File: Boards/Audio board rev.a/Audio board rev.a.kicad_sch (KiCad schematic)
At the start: 65 parts

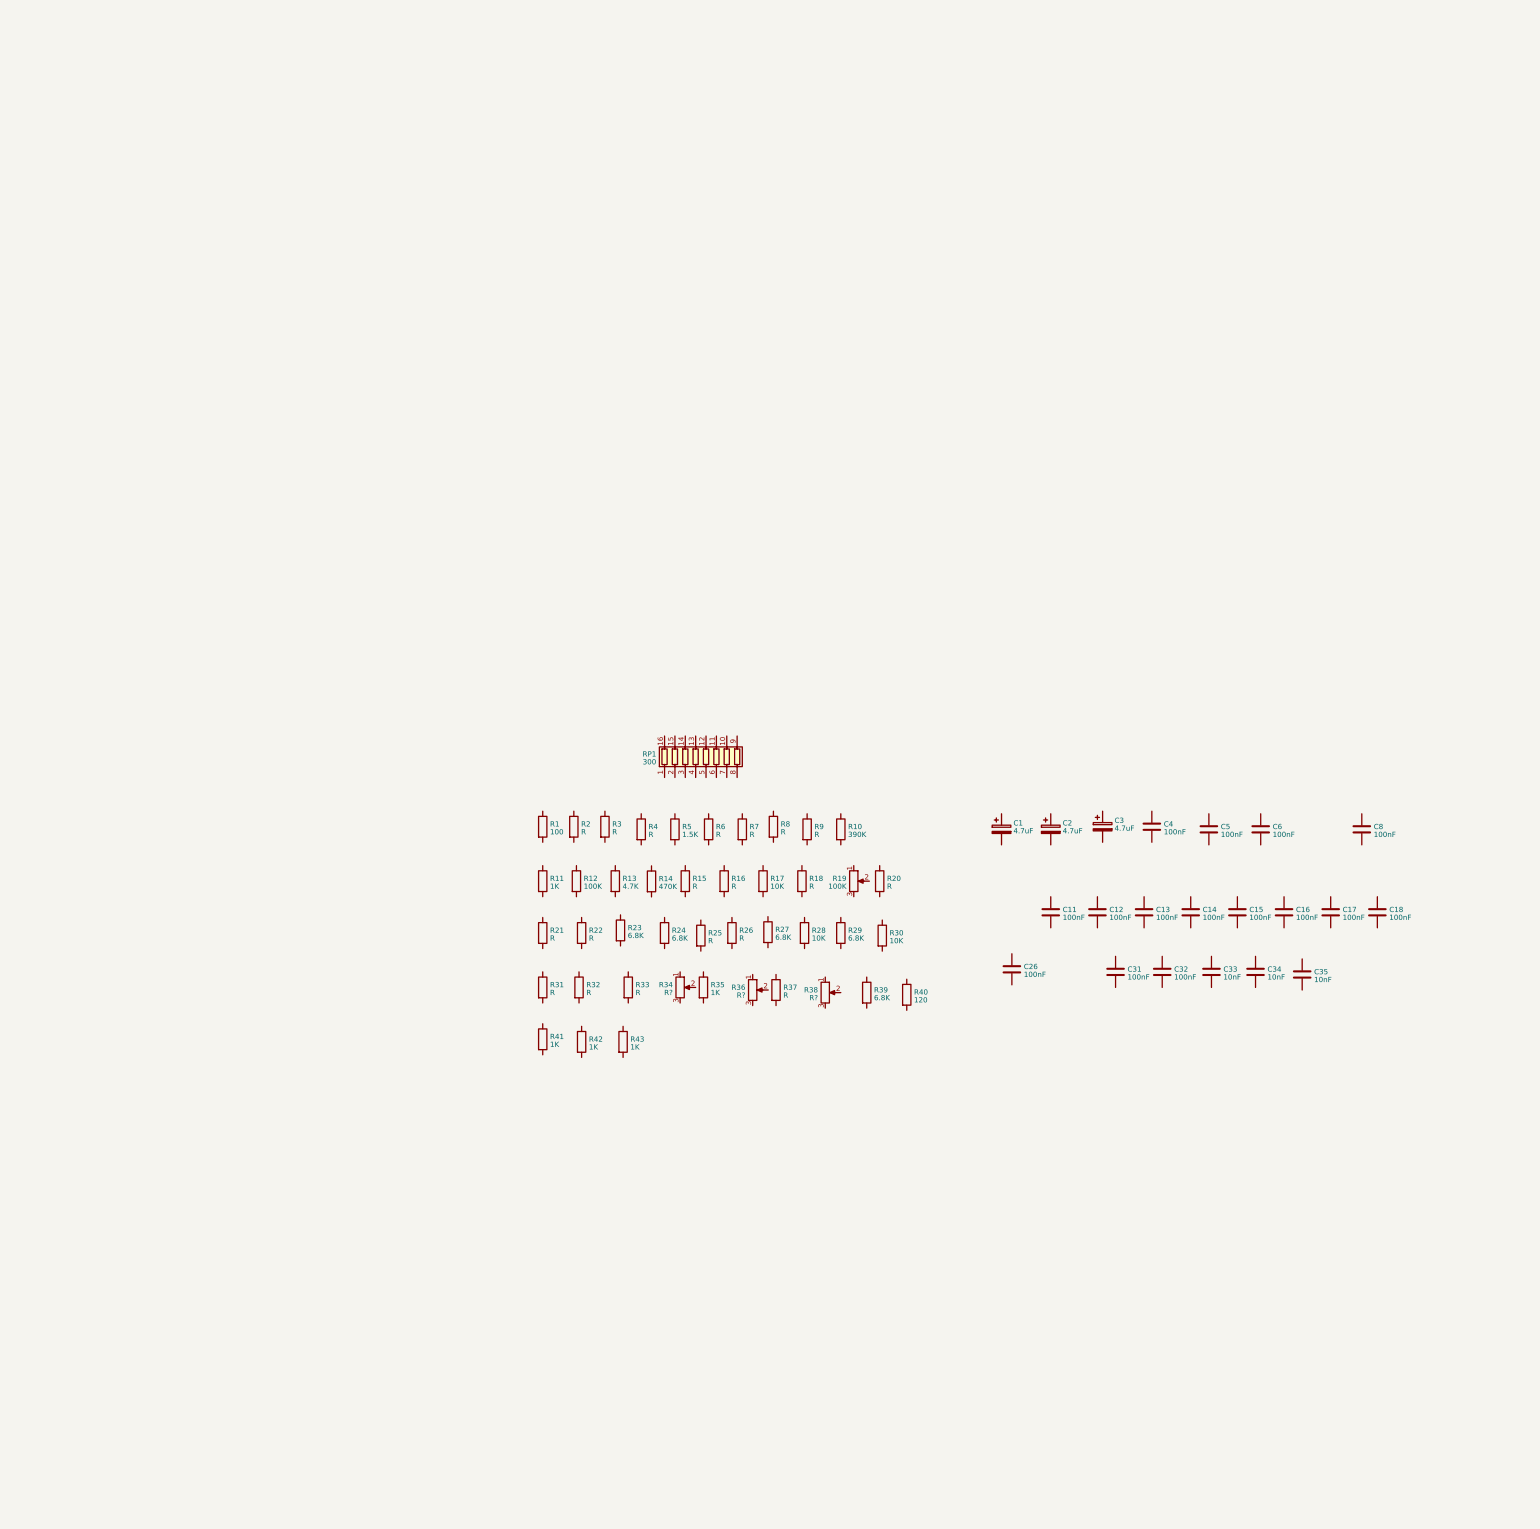
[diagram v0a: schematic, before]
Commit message: audio board rev a agc circuit probably complete
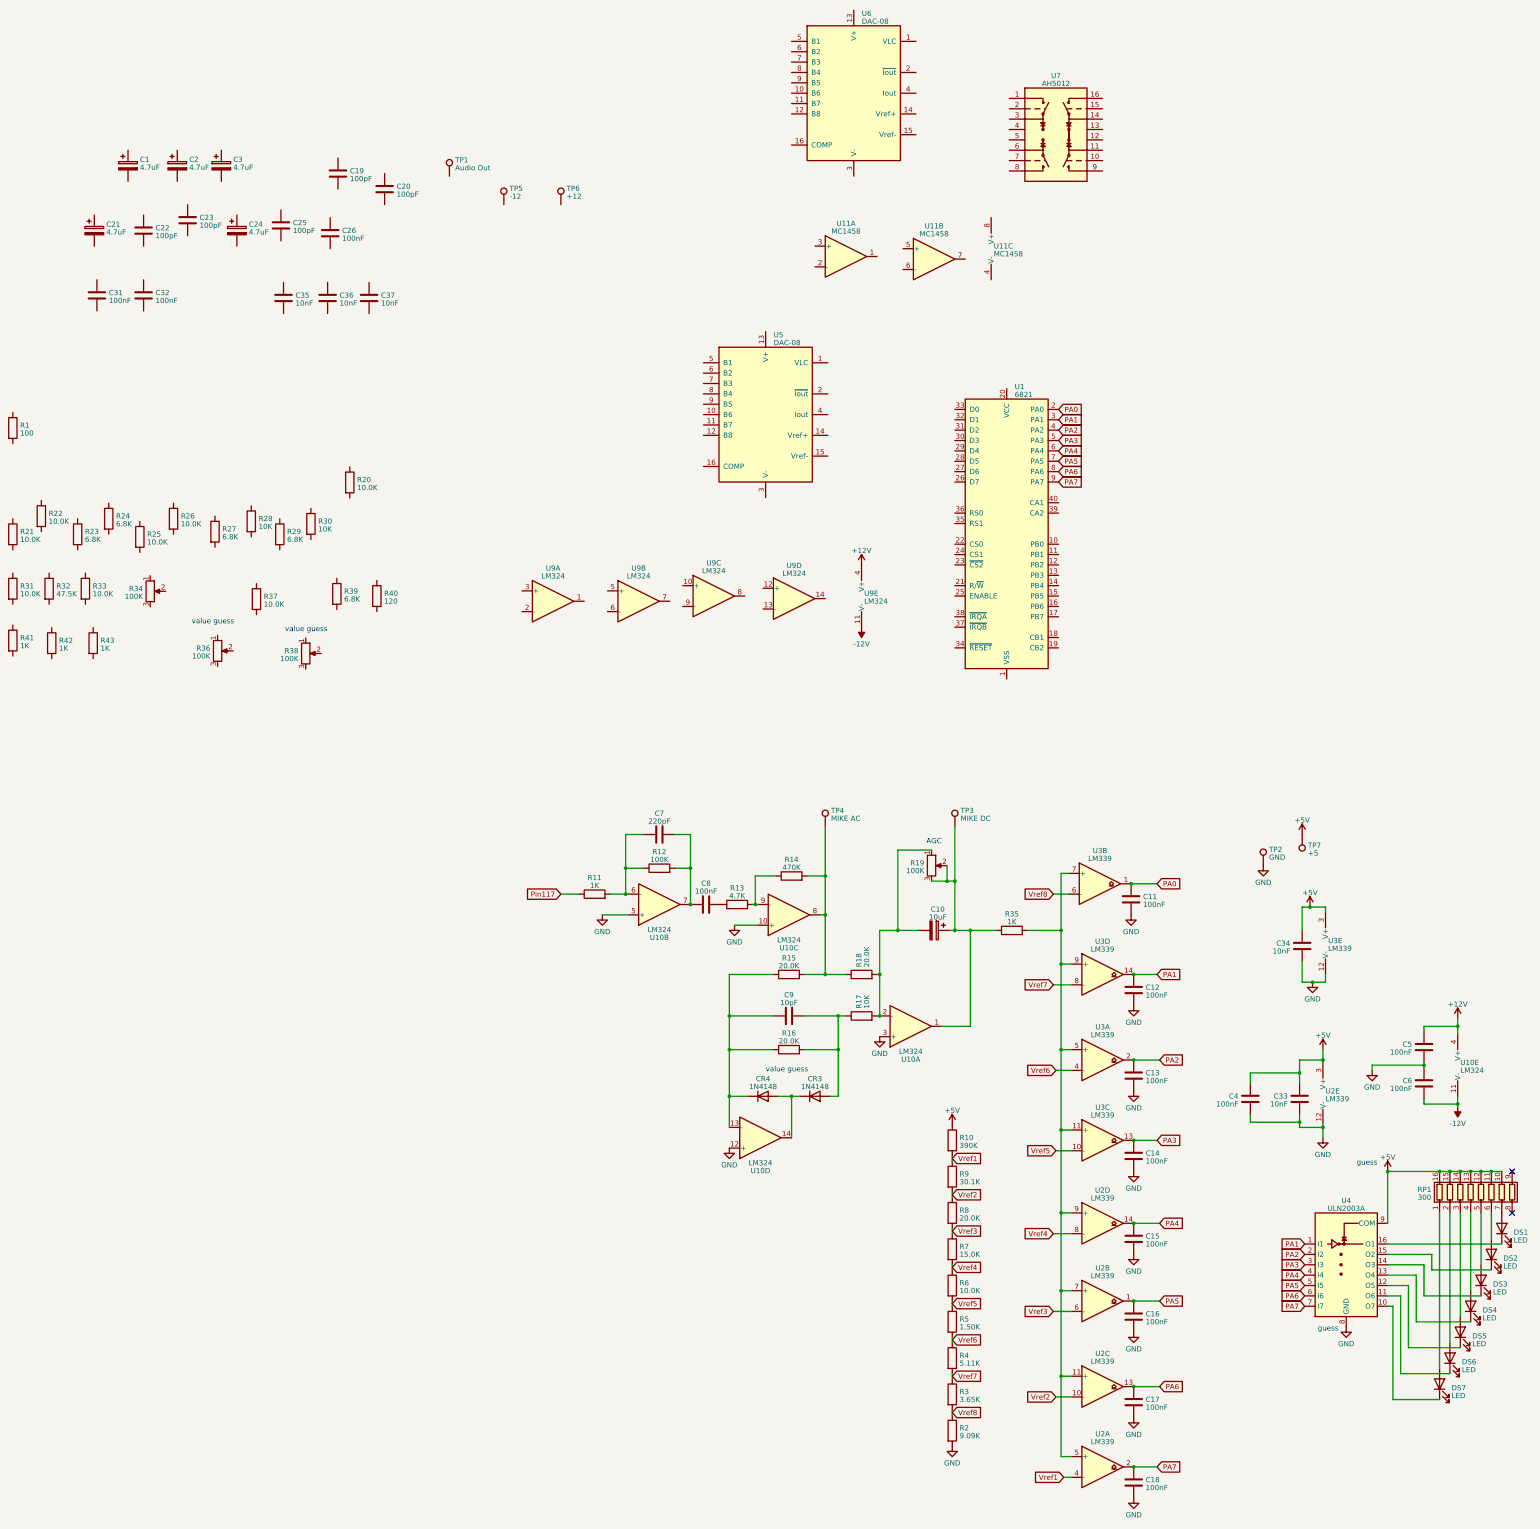
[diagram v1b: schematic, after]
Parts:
- added C10: 10uF, symbol Device:C_Polarized
- added C19, C20, C22, C23, C25: 100pF, symbol Device:C
- added C21, C24: 4.7uF, symbol Device:C_Polarized
- added C36, C37: 10nF, symbol Device:C
- added C7: 220pF, symbol Device:C
- added C9: 10pF, symbol Device:C
- added CR3, CR4: 1N4148, Diode_THT:D_DO-35_SOD27_P7.62mm_Horizontal, symbol Diode:1N4148
- added DS1, DS2, DS3, DS4, DS5, DS6, DS7: LED, symbol Device:LED
- added TP1: Audio Out, symbol Connector:TestPoint
- added TP2: GND, symbol Connector:TestPoint
- added TP3: MIKE DC, symbol Connector:TestPoint
- added TP4: MIKE AC, symbol Connector:TestPoint
- added TP5: -12, symbol Connector:TestPoint
- added TP6: +12, symbol Connector:TestPoint
- added TP7: +5, symbol Connector:TestPoint
- added U1: 6821, Package_DIP:DIP-40_W15.24mm, symbol Interface:6821
- added U10, U9: LM324, symbol Amplifier_Operational:LM324
- added U11: MC1458, symbol Evan's parts:MC1458
- added U2, U3: LM339, symbol Comparator:LM339
- added U4: ULN2003A, symbol Transistor_Array:ULN2003A
- added U5, U6: DAC-08, symbol Evan's parts:DAC-08
- added U7: AH5012, symbol Evan's parts:AH5012
- R15, R16, R18, R8: value R -> 20.0K
- R2: value R -> 9.09K
- R20, R21, R22, R25, R26, R31, R33, R37, R6: value R -> 10.0K
- R3: value R -> 3.65K
- R32: value R -> 47.5K
- R34, R36, R38: value R? -> 100K
- R4: value R -> 5.11K
- R5: value 1.5K -> 1.50K
- R7: value R -> 15.0K
- R9: value R -> 30.1K
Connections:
- net +5V: now reaches C34.1
- net +5V: now also C33.1, C4.1, R10.1, RP1.10 (R7.2), RP1.11 (R6.2), RP1.12 (R5.2), RP1.13 (R4.2), RP1.14 (R3.2), RP1.15 (R2.2), RP1.16 (R1.2), TP7.1, U2.3 (V+), U3.3 (V+), U4.9 (COM)
- net GND: now reaches C34.2
- net GND: now also C11.2, C12.2, C13.2, C14.2, C15.2, C16.2, C17.2, C18.2, C33.2, C4.2, C5.2, C6.1, R2.2, TP2.1, U10.10 (+), U10.12 (+), U10.3 (+), U10.5 (+), U2.12 (V-), U3.12 (V-), U4.8 (GND)
- net Vref8: now reaches R2.1
- net Vref8: now also R3.2, U3.6 (-)
- net PA1: now reaches C12.1
- net PA1: now also U1.3 (PA1), U3.14, U4.1 (I1)
- net Vref7: now reaches R3.1
- net Vref7: now also R4.2, U3.8 (-)
- net at C8.1: now also R12.2, C7.2, U10.7
- net at C8.2: now also R13.1
- net PA7: now reaches C18.1
- net PA7: now also U1.9 (PA7), U2.2, U4.7 (I7)
- net at RP1.1 (R1.1): now also DS7.2 (A)
- net at RP1.2 (R2.1): now also DS6.2 (A)
- net at RP1.3 (R3.1): now also DS5.2 (A)
- net at RP1.4 (R4.1): now also DS4.2 (A)
- net at RP1.5 (R5.1): now also DS3.2 (A)
- net at RP1.6 (R6.1): now also DS2.2 (A)
- net at RP1.7 (R7.1): now also DS1.2 (A)
- net Vref1: now reaches R9.1
- net Vref1: now also R10.2, U2.4 (-)
- net Vref2: now reaches R9.2
- net Vref2: now also R8.1, U2.10 (-)
- net at R16.1: now also R15.1, C9.1, CR4.1 (K), U10.13 (-)
- net at R16.2: now also R17.1, C9.2, CR3.2 (A)
- net PA6: now reaches C17.1
- net PA6: now also U1.8 (PA6), U2.13, U4.6 (I6)
- net -12V: now reaches C6.2
- net -12V: now also U10.11 (V-), U9.11 (V-)
- net at R15.2: now also R14.2, R18.1, TP4.1, U10.8
- net at R35.1: now also R19.2, R19.3, C10.1, TP3.1, U10.1
- net at R35.2: now also U2.11 (+), U2.5 (+), U2.7 (+), U2.9 (+), U3.11 (+), U3.5 (+), U3.7 (+), U3.9 (+)
- net +12V: now reaches C5.1
- net +12V: now also U10.4 (V+), U9.4 (V+)
- net Vref3: now reaches R8.2
- net Vref3: now also R7.1, U2.6 (-)
- net PA4: now reaches C15.1
- net PA4: now also U1.6 (PA4), U2.14, U4.4 (I4)
- net Vref5: now reaches R5.1
- net Vref5: now also R6.2, U3.10 (-)
- net Vref6: now reaches R5.2
- net Vref6: now also R4.1, U3.4 (-)
- net at R14.1: now also R13.2, U10.9 (-)
- net at R19.1: now also R17.2, R18.2, C10.2, U10.2 (-)
- net PA2: now reaches C13.1
- net PA2: now also U1.4 (PA2), U3.2, U4.2 (I2)
- net Pin117: now reaches R11.1
- net at R11.2: now also R12.1, C7.1, U10.6 (-)
- net PA3: now reaches C14.1
- net PA3: now also U1.5 (PA3), U3.13, U4.3 (I3)
- net PA0: now reaches C11.1
- net PA0: now also U1.2 (PA0), U3.1
- net Vref4: now reaches R6.1
- net Vref4: now also R7.2, U2.8 (-)
- net PA5: now reaches C16.1
- net PA5: now also U1.7 (PA5), U2.1, U4.5 (I5)
- new net: CR3.1 (K), CR4.2 (A), U10.14
- new net: DS1.1 (K), U4.16 (O1)
- new net: DS2.1 (K), U4.15 (O2)
- new net: DS3.1 (K), U4.14 (O3)
- new net: DS5.1 (K), U4.12 (O5)
- new net: DS7.1 (K), U4.10 (O7)
- new net: DS6.1 (K), U4.11 (O6)
- new net: DS4.1 (K), U4.13 (O4)
- no-connect marks 0 -> 2
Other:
- note added: "AGC"
- note added: "guess"
- note added: "value guess"
- moved on the sheet: C1, C11, C12, C13, C14, C15, C16, C17, C18, C2, C26, C3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

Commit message: sorted out U11 and some of the card edge
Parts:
- added J1: CEC card edge connector large, symbol Evan's parts:CEC card edge connector large
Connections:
- net +12V: now also C2.1, TP6.1, U11.8 (V+), J1.100 (Pin_100), J1.23 (Pin_23)
- net +5V: now also C1.1, J1.1 (Pin_1), J1.122 (Pin_122)
- net -12V: now also C3.2, TP5.1, U11.4 (V-), J1.101 (Pin_101), J1.22 (Pin_22)
- net GND: now also C1.2, C2.2, C3.1, R38.3, U1.1 (VSS), U11.3 (+), U11.5 (+), J1.106 (Pin_106), J1.108 (Pin_108), J1.11 (Pin_11), J1.110 (Pin_110), J1.112 (Pin_112), J1.114 (Pin_114), J1.116 (Pin_116), J1.118 (Pin_118), J1.121 (Pin_121), J1.13 (Pin_13), J1.15 (Pin_15), J1.17 (Pin_17), J1.2 (Pin_2), J1.27 (Pin_27), J1.36 (Pin_36), J1.5 (Pin_5), J1.54 (Pin_54), J1.55 (Pin_55), J1.56 (Pin_56), J1.57 (Pin_57), J1.58 (Pin_58), J1.59 (Pin_59), J1.60 (Pin_60), J1.61 (Pin_61), J1.7 (Pin_7), J1.87 (Pin_87), J1.9 (Pin_9), J1.96 (Pin_96)
- net at R37.1: now also R36.1, U11.6 (-)
- net Pin 65: now reaches R37.2
- net Pin 65: now also J1.65 (Pin_65)
- net at R20.1: now also R21.1, R22.1, U11.2 (-)
- net Pin 109: now reaches R20.2
- net Pin 109: now also J1.109 (Pin_109), J1.14 (Pin_14)
- net R/~{W}: now reaches U1.21 (R/~{W})
- net R/~{W}: now also J1.66 (Pin_66)
- net at U1.22 (CS0): now also U1.24 (CS1)
- net /CS: now reaches U1.23 (~{CS2})
- net /CS: now also J1.78 (Pin_78)
- net E: now reaches U1.25 (ENABLE)
- net E: now also J1.68 (Pin_68)
- net D7: now reaches U1.26 (D7)
- net D7: now also J1.74 (Pin_74)
- net D6: now reaches U1.27 (D6)
- net D6: now also J1.49 (Pin_49)
- net D5: now reaches U1.28 (D5)
- net D5: now also J1.73 (Pin_73)
- net D4: now reaches U1.29 (D4)
- net D4: now also J1.50 (Pin_50)
- net D3: now reaches U1.30 (D3)
- net D3: now also J1.72 (Pin_72)
- net D2: now reaches U1.31 (D2)
- net D2: now also J1.51 (Pin_51)
- net D1: now reaches U1.32 (D1)
- net D1: now also J1.71 (Pin_71)
- net D0: now reaches U1.33 (D0)
- net D0: now also J1.52 (Pin_52)
- net /RESET: now reaches U1.34 (~{RESET})
- net /RESET: now also J1.67 (Pin_67)
- net RS1: now reaches U1.35 (RS1)
- net RS1: now also J1.47 (Pin_47)
- net RS0: now reaches U1.36 (RS0)
- net RS0: now also J1.75 (Pin_75)
- net Pin 18: now reaches U11.7
- net Pin 18: now also R36.2, R36.3, J1.18 (Pin_18)
- net at R21.2: now also R38.2
- net at U5.15 (Vref-): now also R22.2, U11.1
- net Pin 107: now reaches R38.1
- net Pin 107: now also J1.107 (Pin_107), J1.16 (Pin_16)
- net Pin117 renamed Mike
- net Mike: now also J1.117 (Pin_117)
- no-connect marks 2 -> 59
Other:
- note added: "GAME RM OUT"
- note added: "MUSIC IN"
- moved on the sheet: C1, C2, C3, R20, R21, R22, R36, R37, R38, TP2, TP5, TP6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

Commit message: working on U9 section
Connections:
- net +12V: now also C31.2
- net +5V: now also C35.1
- net -12V: now also C32.1
- net GND: now also C31.1, C32.2, C35.2
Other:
- moved on the sheet: C20, C21, C23, C24, C25, C26, C31, C32, C35, C36, C37, R27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

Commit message: half of u9 done
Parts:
- R39: value 6.8K -> 1K
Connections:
- net +12V: now also R39.1, R43.2
- net GND: now also U9.3 (+), U9.5 (+)
- net at R43.1: now also R34.3, R40.1, U9.1
- net Pin 120: now reaches R40.2
- net Pin 120: now also J1.120 (Pin_120), J1.3 (Pin_3), TP1.1
- net at R32.1: now also C26.2
- net at R32.2: now also R33.2, U9.2 (-)
- net at R31.1: now also C25.1, C26.1, U9.7
- net at R31.2: now also C25.2, R39.2, U7.16, U7.9, U9.6 (-)
- net at R34.1: now also R33.1, R34.2
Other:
- note added: "AUDIO OUT"
- note added: "connections under resistor unknown"
- moved on the sheet: C25, C26, R31, R32, R33, R34, R39, R40, R43, TP1, U7, U9A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

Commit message: finished initial layout and added backplane notes from san jose trip
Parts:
- R1: value 100 -> 10K
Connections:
- net +12V: now also J1.39 (Pin_39), R41.1, R42.1, U5.13 (V+), U6.13 (V+); no longer J1.23 (Pin_23)
- net +5V: now also J1.61 (Pin_61), R1.1, R23.1, R24.1, U1.20 (VCC); no longer J1.1 (Pin_1)
- net -12V: now also C19.2, C22.2, J1.40 (Pin_40), U5.3 (V-), U6.3 (V-); no longer J1.22 (Pin_22)
- net D0: now also J1.10 (Pin_10); no longer J1.52 (Pin_52)
- net D2: now also J1.11 (Pin_11); no longer J1.51 (Pin_51)
- net D4: now also J1.12 (Pin_12); no longer J1.50 (Pin_50)
- net D6: now also J1.13 (Pin_13); no longer J1.49 (Pin_49)
- net GND: now also C36.1, C37.1, J1.1 (Pin_1), J1.26 (Pin_26), J1.3 (Pin_3), J1.35 (Pin_35), J1.4 (Pin_4), J1.45 (Pin_45), J1.47 (Pin_47), J1.49 (Pin_49), J1.51 (Pin_51), J1.53 (Pin_53), J1.6 (Pin_6), J1.8 (Pin_8), R28.2, R30.1, U5.1 (VLC), U5.2 (~{Iout}), U6.1 (VLC), U6.2 (~{Iout}), U7.12, U7.13, U7.4, U7.5, U9.10 (+), U9.12 (+); no longer J1.11 (Pin_11), J1.13 (Pin_13), J1.15 (Pin_15), J1.17 (Pin_17), J1.27 (Pin_27), J1.36 (Pin_36), J1.54 (Pin_54), J1.56 (Pin_56), J1.58 (Pin_58), J1.59 (Pin_59), J1.61 (Pin_61), J1.9 (Pin_9)
- net Pin 65: now also R26.2, U7.14
- net RS1: now also J1.15 (Pin_15); no longer J1.47 (Pin_47)
- net at R27.1: now also C20.1, C36.2, U5.4 (Iout), U9.13 (-)
- net at R27.2: now also C20.2, C21.1, R42.2, U9.14
- net at R29.1: now also C23.1, C37.2, U6.4 (Iout), U9.9 (-)
- net at R29.2: now also C23.2, C24.1, R41.2, U9.8
- net PB2: now reaches U6.10 (B6)
- net PB2: now also U1.12 (PB2), U5.10 (B6)
- net PB1: now reaches U6.11 (B7)
- net PB1: now also U1.11 (PB1), U5.11 (B7)
- net PB0: now reaches U6.12 (B8)
- net PB0: now also U1.10 (PB0), U5.12 (B8)
- net at U6.14 (Vref+): now also R24.2
- net R2R_audio_track: now reaches U6.15 (Vref-)
- net R2R_audio_track: now also J1.111 (Pin_111), J1.50 (Pin_50)
- net at U6.16 (COMP): now also C19.1
- net PB7: now reaches U6.5 (B1)
- net PB7: now also U1.17 (PB7), U5.5 (B1)
- net PB6: now reaches U6.6 (B2)
- net PB6: now also U1.16 (PB6), U5.6 (B2)
- net PB5: now reaches U6.7 (B3)
- net PB5: now also U1.15 (PB5), U5.7 (B3)
- net PB4: now reaches U6.8 (B4)
- net PB4: now also U1.14 (PB4), U5.8 (B4)
- net PB3: now reaches U6.9 (B5)
- net PB3: now also U1.13 (PB3), U5.9 (B5)
- net at R1.2: now also U1.22 (CS0), U1.24 (CS1)
- net CB1: now reaches U1.18 (CB1)
- net CB1: now also U7.15
- net CB2: now reaches U1.19 (CB2)
- net CB2: now also U7.10
- net Pin 113: now reaches J1.113 (Pin_113)
- net Pin 113: now also J1.52 (Pin_52)
- net Pin 115: now reaches J1.115 (Pin_115)
- net Pin 115: now also J1.54 (Pin_54)
- net BGOUT: now reaches J1.44 (Pin_44)
- net BGOUT: now also R36.2, R36.3, U11.7
- net BGIN: now reaches J1.46 (Pin_46)
- net BGIN: now also J1.107 (Pin_107), R38.1
- net MIKEIN: now reaches J1.48 (Pin_48)
- net MIKEIN: now also J1.109 (Pin_109), R20.2
- net Pin 64: now reaches J1.64 (Pin_64)
- net Pin 64: now also R25.2, U7.11
- net at C21.2: now also R26.1, R28.1
- net at R23.2: now also U5.14 (Vref+)
- net at C22.1: now also U5.16 (COMP)
- net at R30.2: now also C24.2, R25.1
- net Mike renamed AGCMIC
- net AGCMIC: now also J1.56 (Pin_56)
- removed net Pin 107: J1.107 (Pin_107), J1.16 (Pin_16), R38.1
- removed net Pin 109: J1.109 (Pin_109), J1.14 (Pin_14), R20.2
- net Pin 120 renamed AUDOUT
- net AUDOUT: now also J1.59 (Pin_59); no longer J1.3 (Pin_3)
- removed net Pin 18: J1.18 (Pin_18), R36.2, R36.3, U11.7
- no-connect marks 59 -> 69
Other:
- note added: "only jumps 113 to 52"
- note added: "only jumps 115 to 54"
- moved on the sheet: C1, C2, C20, C21, C22, C23, C24, C25, C26, C3, C31, C32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

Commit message: fixed resistor value, moved bgaudio amp to logical location
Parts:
- R5: value 1.50K -> 7.50K
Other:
- moved on the sheet: R36, R37, U11B

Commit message: board outline done, picking footprints
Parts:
- C11, C12, C13, C14, C15, C16, C17, C18, C26, C31, C32, C4, C5, C6, C8: footprint (none) -> Capacitor_THT:C_Disc_D3.0mm_W1.6mm_P2.50mm
- C33, C34, C35: footprint (none) -> Capacitor_THT:C_Rect_L9.0mm_W2.5mm_P7.50mm_MKT
- DS1, DS2, DS3, DS4, DS5, DS6, DS7: footprint (none) -> LED_THT:LED_D5.0mm_Horizontal_O3.81mm_Z15.0mm
- J1: footprint (none) -> Evan's parts:Chuck_E_Cheese_large_card_edge
- R1, R10, R11, R12, R13, R14, R15, R16, R17, R18, R2, R20, R21, R22, R23, R24, R25, R26, R27, R28, R29, R3, R30, R31, R32, R33, R35, R37, R39, R4, R40, R41, R42, R43, R5, R6, R7, R8, R9: footprint (none) -> Resistor_THT:R_Axial_DIN0309_L9.0mm_D3.2mm_P12.70mm_Horizontal
- RP1, U4, U5, U6, U7: footprint (none) -> Package_DIP:DIP-16_W7.62mm
- TP1, TP2, TP3, TP4, TP5, TP6, TP7: footprint (none) -> TestPoint:TestPoint_Plated_Hole_D3.0mm
- U10, U2, U3, U9: footprint (none) -> Package_DIP:DIP-14_W7.62mm
- U11: footprint (none) -> Package_DIP:DIP-8_W7.62mm
